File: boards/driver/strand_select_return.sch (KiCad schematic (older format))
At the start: 88 parts, among them Q24 NPN, Q25 NPN, Q26 NPN, Q27 PMOS, Q28 PMOS, Q29 PMOS, Q30 NPN, Q31 NPN, Q32 NPN, Q33 PMOS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

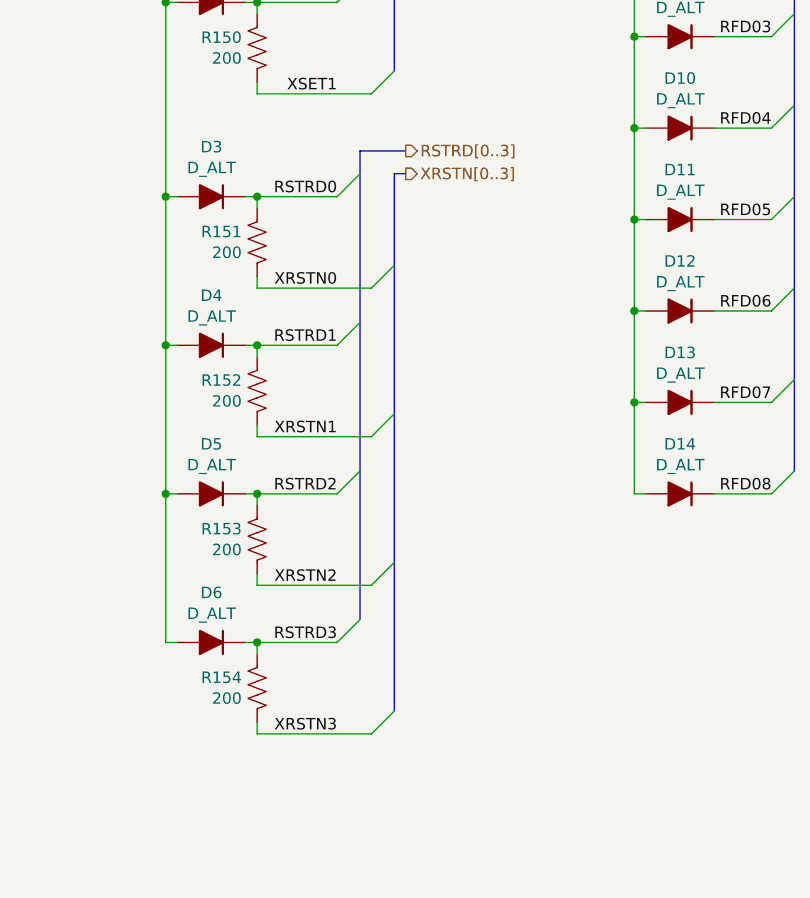
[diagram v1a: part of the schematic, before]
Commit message: Driver boards: filled out all of the FPGA connections. Power circuits to still be defined.
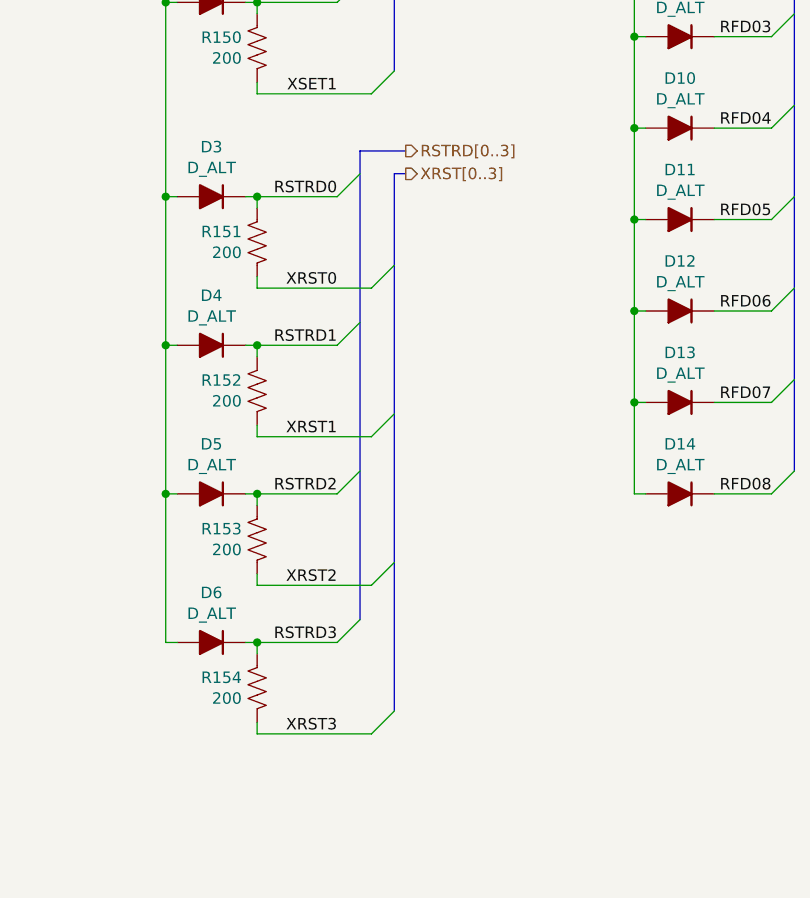
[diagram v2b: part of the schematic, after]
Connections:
- net XRSTN0 renamed XRST0
- net XRSTN1 renamed XRST1
- net XRSTN2 renamed XRST2
- net XRSTN3 renamed XRST3
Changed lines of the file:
@@
 RSTRD0
 Text Label 11600 4750 2    50   ~ 0
-XRSTN0
+XRST0
 Entry Wire Line
 	11600 4350 11700 4250
@@
 RSTRD1
 Text Label 11600 5400 2    50   ~ 0
-XRSTN1
+XRST1
 Entry Wire Line
 	11600 5000 11700 4900
@@
 RSTRD2
 Text Label 11600 6050 2    50   ~ 0
-XRSTN2
+XRST2
 Entry Wire Line
 	11600 5650 11700 5550
@@
 RSTRD3
 Text Label 11600 6700 2    50   ~ 0
-XRSTN3
+XRST3
 Entry Wire Line
 	11600 6300 11700 6200
@@
 RSTRD[0..3]
 Text HLabel 11900 4250 2    50   Output ~ 0
-XRSTN[0..3]
+XRST[0..3]
 Wire Bus Line
 	13600 2650 13650 2650
